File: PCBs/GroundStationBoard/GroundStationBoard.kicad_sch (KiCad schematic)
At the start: 2 parts

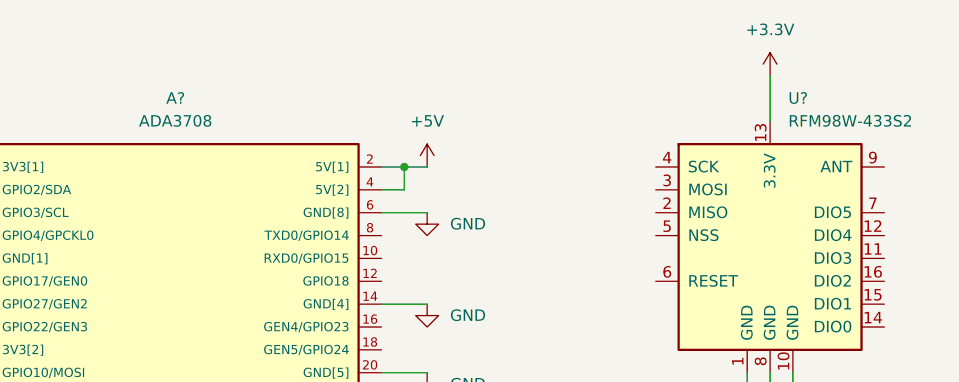
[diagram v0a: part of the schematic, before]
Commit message: 4 layer-ifying the PCB, traces, board cuts and trace width
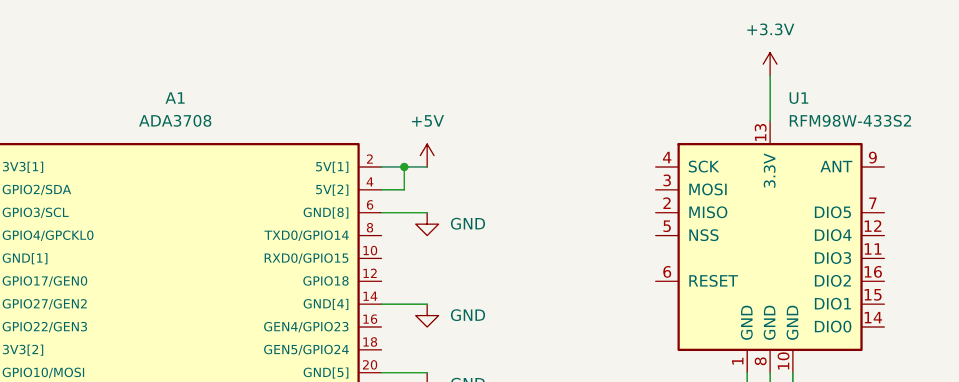
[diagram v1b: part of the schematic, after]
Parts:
- gave numbers to parts that had none: 2
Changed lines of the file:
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@@
   (symbol (lib_id "RF_Module:RFM98W-433S2") (at 187.96 86.36 0) (unit 1)
     (in_bom yes) (on_board yes) (fields_autoplaced)
-    (property "Reference" "U?" (id 0) (at 189.9794 71.12 0)
+    (property "Reference" "U1" (id 0) (at 189.9794 71.12 0)
       (effects (font (size 1.27 1.27)) (justify left))
     )
@@
   (symbol (lib_id "power:GND") (at 187.96 106.68 0) (unit 1)
     (in_bom yes) (on_board yes) (fields_autoplaced)
-    (property "Reference" "#PWR?" (id 0) (at 187.96 113.03 0)
+    (property "Reference" "#PWR0106" (id 0) (at 187.96 113.03 0)
       (effects (font (size 1.27 1.27)) hide)
     )
@@
   (symbol (lib_id "power:GND") (at 149.86 93.98 0) (unit 1)
     (in_bom yes) (on_board yes) (fields_autoplaced)
-    (property "Reference" "#PWR?" (id 0) (at 149.86 100.33 0)
+    (property "Reference" "#PWR0104" (id 0) (at 149.86 100.33 0)
       (effects (font (size 1.27 1.27)) hide)
     )
@@
   (symbol (lib_id "power:GND") (at 149.86 83.82 0) (unit 1)
     (in_bom yes) (on_board yes) (fields_autoplaced)
-    (property "Reference" "#PWR?" (id 0) (at 149.86 90.17 0)
+    (property "Reference" "#PWR0107" (id 0) (at 149.86 90.17 0)
       (effects (font (size 1.27 1.27)) hide)
     )
@@
   (symbol (lib_id "ADA3708:ADA3708") (at 121.92 101.6 0) (unit 1)
     (in_bom yes) (on_board yes) (fields_autoplaced)
-    (property "Reference" "A?" (id 0) (at 121.92 71.12 0))
+    (property "Reference" "A1" (id 0) (at 121.92 71.12 0))
     (property "Value" "ADA3708" (id 1) (at 121.92 73.66 0))
     (property "Footprint" "ADA3708_RPI-ZERO" (id 2) (at 121.92 101.6 0)
@@
   (symbol (lib_id "power:GND") (at 93.98 88.9 0) (unit 1)
     (in_bom yes) (on_board yes) (fields_autoplaced)
-    (property "Reference" "#PWR?" (id 0) (at 93.98 95.25 0)
+    (property "Reference" "#PWR0109" (id 0) (at 93.98 95.25 0)
       (effects (font (size 1.27 1.27)) hide)
     )
@@
   (symbol (lib_id "power:GND") (at 149.86 101.6 0) (unit 1)
     (in_bom yes) (on_board yes) (fields_autoplaced)
-    (property "Reference" "#PWR?" (id 0) (at 149.86 107.95 0)
+    (property "Reference" "#PWR0102" (id 0) (at 149.86 107.95 0)
       (effects (font (size 1.27 1.27)) hide)
     )
@@
   (symbol (lib_id "power:+5V") (at 149.86 78.74 0) (unit 1)
     (in_bom yes) (on_board yes) (fields_autoplaced)
-    (property "Reference" "#PWR?" (id 0) (at 149.86 82.55 0)
+    (property "Reference" "#PWR0108" (id 0) (at 149.86 82.55 0)
       (effects (font (size 1.27 1.27)) hide)
     )
@@
   (symbol (lib_id "power:+3.3V") (at 93.98 78.74 0) (unit 1)
     (in_bom yes) (on_board yes) (fields_autoplaced)
-    (property "Reference" "#PWR?" (id 0) (at 93.98 82.55 0)
+    (property "Reference" "#PWR0110" (id 0) (at 93.98 82.55 0)
       (effects (font (size 1.27 1.27)) hide)
     )
@@
   (symbol (lib_id "power:GND") (at 93.98 109.22 0) (unit 1)
     (in_bom yes) (on_board yes) (fields_autoplaced)
-    (property "Reference" "#PWR?" (id 0) (at 93.98 115.57 0)
+    (property "Reference" "#PWR0113" (id 0) (at 93.98 115.57 0)
       (effects (font (size 1.27 1.27)) hide)
     )
@@
   (symbol (lib_id "power:+3.3V") (at 93.98 99.06 0) (unit 1)
     (in_bom yes) (on_board yes) (fields_autoplaced)
-    (property "Reference" "#PWR?" (id 0) (at 93.98 102.87 0)
+    (property "Reference" "#PWR0111" (id 0) (at 93.98 102.87 0)
       (effects (font (size 1.27 1.27)) hide)
     )
@@
   (symbol (lib_id "power:GND") (at 149.86 114.3 0) (unit 1)
     (in_bom yes) (on_board yes) (fields_autoplaced)
-    (property "Reference" "#PWR?" (id 0) (at 149.86 120.65 0)
+    (property "Reference" "#PWR0103" (id 0) (at 149.86 120.65 0)
       (effects (font (size 1.27 1.27)) hide)
     )
@@
   (symbol (lib_id "power:GND") (at 93.98 127 0) (unit 1)
     (in_bom yes) (on_board yes) (fields_autoplaced)
-    (property "Reference" "#PWR?" (id 0) (at 93.98 133.35 0)
+    (property "Reference" "#PWR0112" (id 0) (at 93.98 133.35 0)
       (effects (font (size 1.27 1.27)) hide)
     )
@@
   (symbol (lib_id "power:GND") (at 149.86 119.38 0) (unit 1)
     (in_bom yes) (on_board yes) (fields_autoplaced)
-    (property "Reference" "#PWR?" (id 0) (at 149.86 125.73 0)
+    (property "Reference" "#PWR0105" (id 0) (at 149.86 125.73 0)
       (effects (font (size 1.27 1.27)) hide)
     )
@@
   (symbol (lib_id "power:+3.3V") (at 187.96 68.58 0) (unit 1)
     (in_bom yes) (on_board yes) (fields_autoplaced)
-    (property "Reference" "#PWR?" (id 0) (at 187.96 72.39 0)
+    (property "Reference" "#PWR0101" (id 0) (at 187.96 72.39 0)
       (effects (font (size 1.27 1.27)) hide)
     )
@@
   )
   (symbol_instances
+    (path "/df933423-8150-4da9-a8c1-053c01a26516"
+      (reference "#PWR0101") (unit 1) (value "+3.3V") (footprint "")
+    )
+    (path "/7b4cdddc-eb59-4d1a-a318-0bc56fa5d5d6"
+      (reference "#PWR0102") (unit 1) (value "GND") (footprint "")
+    )
+    (path "/bbeeea0c-2f69-4251-ae25-85b705f29d61"
+      (reference "#PWR0103") (unit 1) (value "GND") (footprint "")
+    )
+    (path "/459906ba-57da-47a8-af63-5c91182f1db4"
+      (reference "#PWR0104") (unit 1) (value "GND") (footprint "")
+    )
+    (path "/c49fcd9b-ea56-4ecf-9c1b-e9ec9bb21f0f"
+      (reference "#PWR0105") (unit 1) (value "GND") (footprint "")
+    )
     (path "/055e68bf-2e0d-4027-9101-e13ae58966b1"
-      (reference "#PWR?") (unit 1) (value "GND") (footprint "")
-    )
-    (path "/459906ba-57da-47a8-af63-5c91182f1db4"
-      (reference "#PWR?") (unit 1) (value "GND") (footprint "")
+      (reference "#PWR0106") (unit 1) (value "GND") (footprint "")
     )
     (path "/58f34631-e4d9-450a-a553-86af09ffce66"
-      (reference "#PWR?") (unit 1) (value "GND") (footprint "")
+      (reference "#PWR0107") (unit 1) (value "GND") (footprint "")
+    )
+    (path "/86075da1-b3fa-4f8a-8587-413c0ba1067f"
+      (reference "#PWR0108") (unit 1) (value "+5V") (footprint "")
     )
     (path "/6a31079a-1c12-428c-82c9-18cc27c44d4e"
-      (reference "#PWR?") (unit 1) (value "GND") (footprint "")
-    )
-    (path "/7b4cdddc-eb59-4d1a-a318-0bc56fa5d5d6"
-      (reference "#PWR?") (unit 1) (value "GND") (footprint "")
-    )
-    (path "/86075da1-b3fa-4f8a-8587-413c0ba1067f"
-      (reference "#PWR?") (unit 1) (value "+5V") (footprint "")
+      (reference "#PWR0109") (unit 1) (value "GND") (footprint "")
     )
     (path "/a1865bc8-c3f3-45b9-a4b6-8c15425f67b8"
-      (reference "#PWR?") (unit 1) (value "+3.3V") (footprint "")
+      (reference "#PWR0110") (unit 1) (value "+3.3V") (footprint "")
+    )
+    (path "/b861cd7a-5dd1-4c28-abf1-5ddf3b207121"
+      (reference "#PWR0111") (unit 1) (value "+3.3V") (footprint "")
+    )
+    (path "/bdf301a0-df44-42fd-bda1-4d44bbf3134e"
+      (reference "#PWR0112") (unit 1) (value "GND") (footprint "")
     )
     (path "/b7da7430-bf45-4ae0-b82e-d44ad1c7a245"
-      (reference "#PWR?") (unit 1) (value "GND") (footprint "")
-    )
-    (path "/b861cd7a-5dd1-4c28-abf1-5ddf3b207121"
-      (reference "#PWR?") (unit 1) (value "+3.3V") (footprint "")
-    )
-    (path "/bbeeea0c-2f69-4251-ae25-85b705f29d61"
-      (reference "#PWR?") (unit 1) (value "GND") (footprint "")
-    )
-    (path "/bdf301a0-df44-42fd-bda1-4d44bbf3134e"
-      (reference "#PWR?") (unit 1) (value "GND") (footprint "")
-    )
-    (path "/c49fcd9b-ea56-4ecf-9c1b-e9ec9bb21f0f"
-      (reference "#PWR?") (unit 1) (value "GND") (footprint "")
-    )
-    (path "/df933423-8150-4da9-a8c1-053c01a26516"
-      (reference "#PWR?") (unit 1) (value "+3.3V") (footprint "")
+      (reference "#PWR0113") (unit 1) (value "GND") (footprint "")
     )
     (path "/695f3645-22ae-40bc-a3f8-3d3b654779fc"
-      (reference "A?") (unit 1) (value "ADA3708") (footprint "ADA3708_RPI-ZERO")
+      (reference "A1") (unit 1) (value "ADA3708") (footprint "ADA3708_RPI-ZERO")
     )
     (path "/0317c931-1204-4016-8917-448af46bbbff"
-      (reference "U?") (unit 1) (value "RFM98W-433S2") (footprint "")
-    )
-  )
+      (reference "U1") (unit 1) (value "RFM98W-433S2") (footprint "")
+    )
+  )

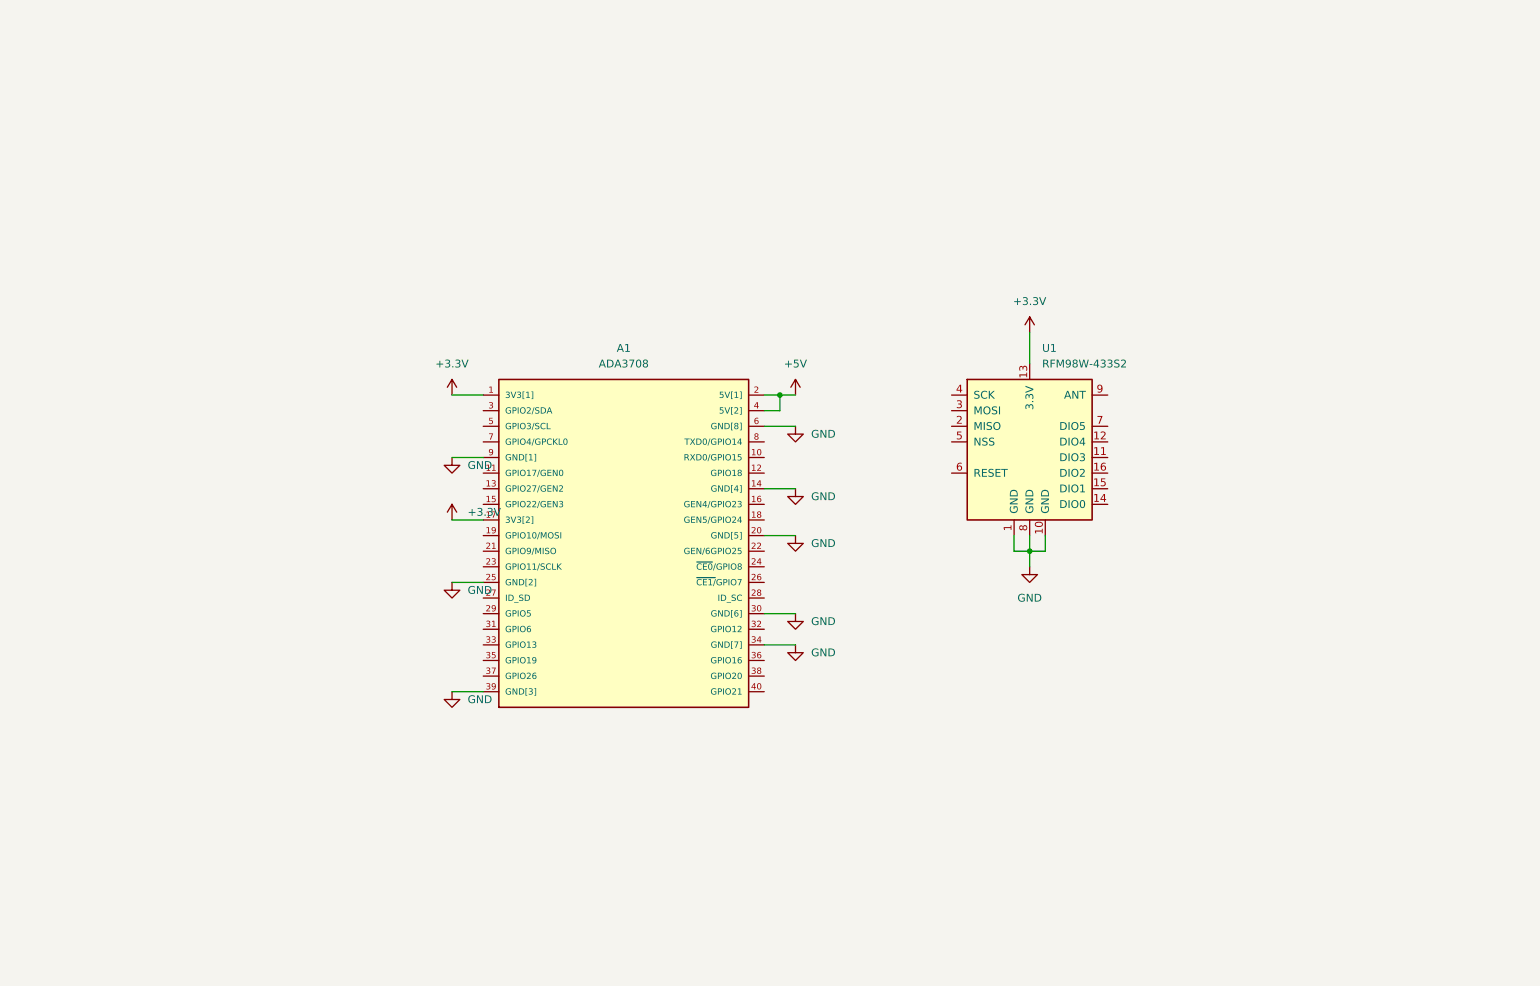
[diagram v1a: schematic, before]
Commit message: added SMA connector and RF switch to schematic
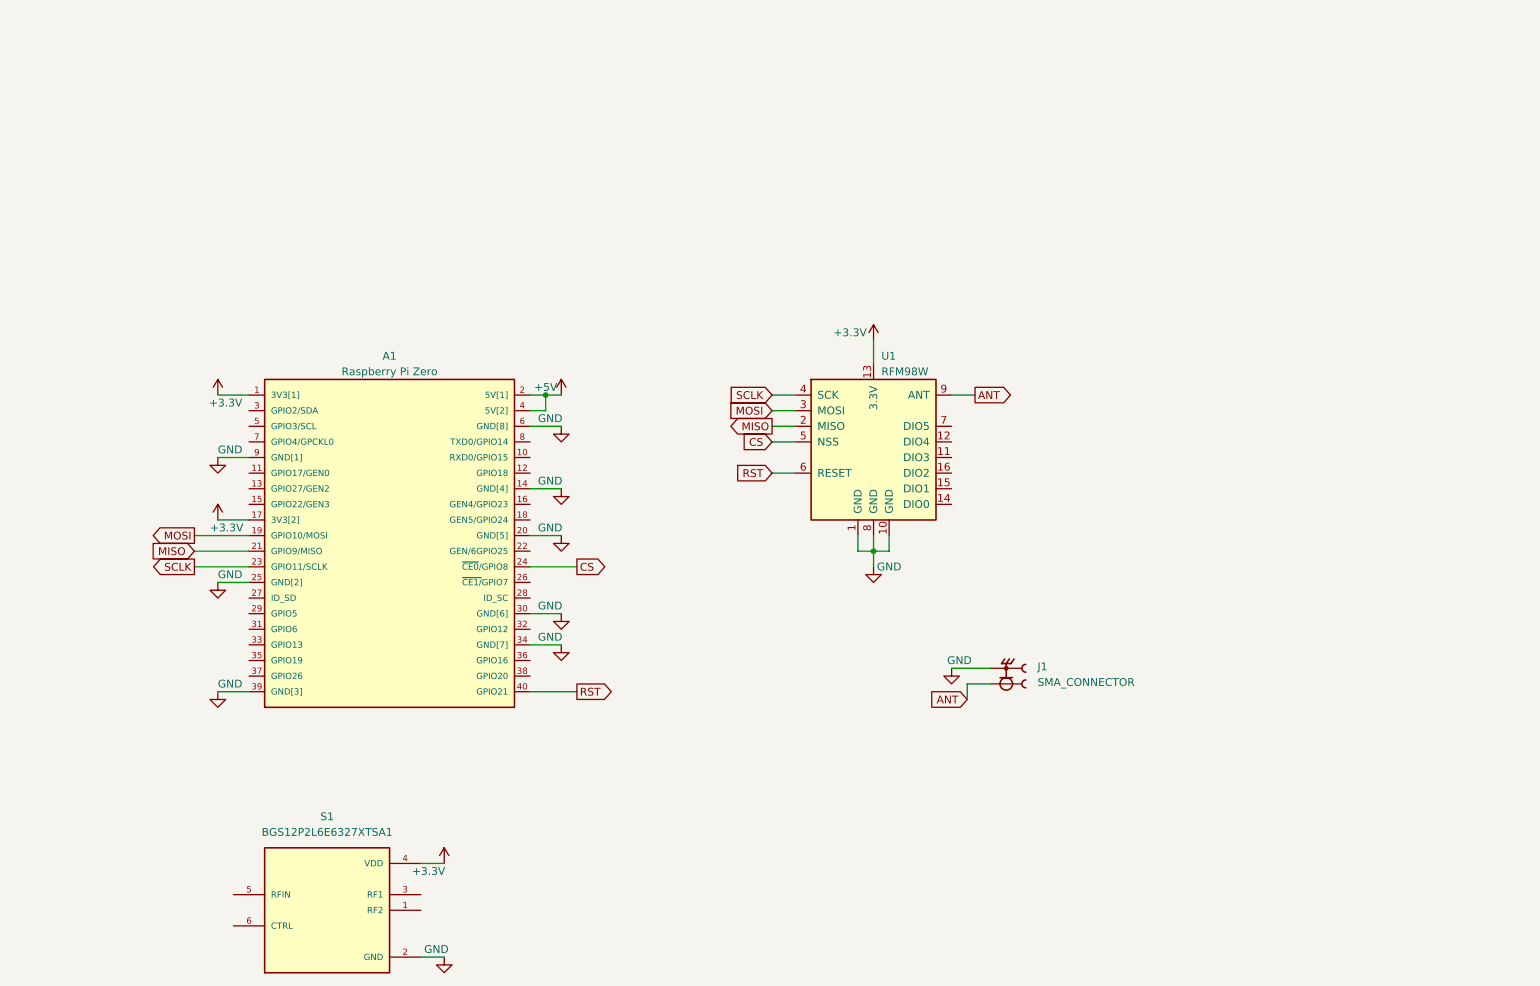
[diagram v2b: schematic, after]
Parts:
- added J1: SMA_CONNECTOR, SMA_CONNECTOR:LPRS_SMA_CONNECTOR, symbol SMA_CONNECTOR:SMA_CONNECTOR
- added S1: BGS12P2L6E6327XTSA1, BGS12P2L6E6327XTSA1:SW_BGS12P2L6E6327XTSA1, symbol BGS12P2L6E6327XTSA1:BGS12P2L6E6327XTSA1
- A1: value ADA3708 -> Raspberry Pi Zero; footprint ADA3708_RPI-ZERO -> ADA3708:ADA3708_RPI-ZERO
- U1: value RFM98W-433S2 -> RFM98W; footprint (none) -> RFM98W-433S2:XCVR_RFM98W-433S2
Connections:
- net +3.3V: now also S1.4 (VDD)
- net GND: now also J1.G1, J1.G2, J1.G3, J1.G4, S1.2 (GND)
- net MISO: now reaches U1.2 (MISO)
- net MISO: now also A1.21 (GPIO9/MISO)
- net MOSI: now reaches U1.3 (MOSI)
- net MOSI: now also A1.19 (GPIO10/MOSI)
- net SCLK: now reaches U1.4 (SCK)
- net SCLK: now also A1.23 (GPIO11/SCLK)
- net CS: now reaches U1.5 (NSS)
- net CS: now also A1.24 (~{CE0}/GPIO8)
- net RST: now reaches U1.6 (RESET)
- net RST: now also A1.40 (GPIO21)
- net ANT: now reaches U1.9 (ANT)
- net ANT: now also J1.1
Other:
- moved on the sheet: A1, U1

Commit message: worked on data I/O pins
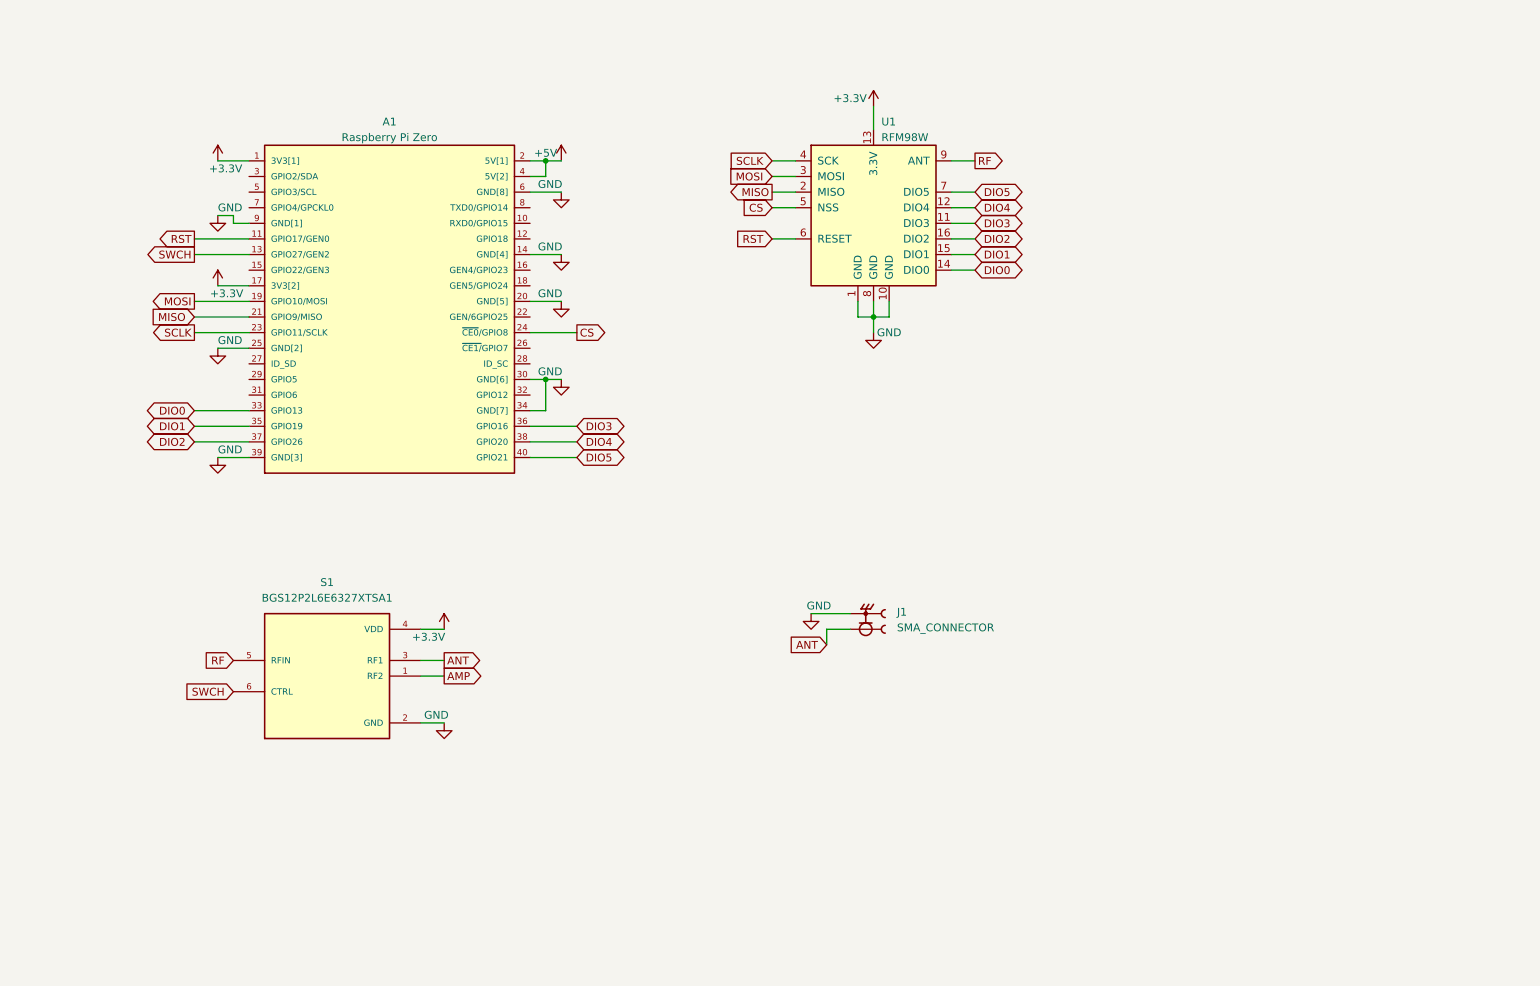
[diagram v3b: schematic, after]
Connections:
- net ANT: now also S1.3 (RF1); no longer U1.9 (ANT)
- net RST: now also A1.11 (GPIO17/GEN0); no longer A1.40 (GPIO21)
- net DIO3: now reaches U1.11 (DIO3)
- net DIO3: now also A1.36 (GPIO16)
- net DIO4: now reaches U1.12 (DIO4)
- net DIO4: now also A1.38 (GPIO20)
- net DIO0: now reaches U1.14 (DIO0)
- net DIO0: now also A1.33 (GPIO13)
- net DIO1: now reaches U1.15 (DIO1)
- net DIO1: now also A1.35 (GPIO19)
- net DIO2: now reaches U1.16 (DIO2)
- net DIO2: now also A1.37 (GPIO26)
- net DIO5: now reaches U1.7 (DIO5)
- net DIO5: now also A1.40 (GPIO21)
- net SWCH: now reaches A1.13 (GPIO27/GEN2)
- net SWCH: now also S1.6 (CTRL)
- net AMP: now reaches S1.1 (RF2)
- net RF: now reaches S1.5 (RFIN)
- net RF: now also U1.9 (ANT)
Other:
- moved on the sheet: A1, J1, S1, U1
